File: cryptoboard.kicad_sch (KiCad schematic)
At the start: 12 parts, among them J1 USB_A, J2 BOOT, U1 STM32F103C8Tx, U2 LM317_SOT-223-3.3V

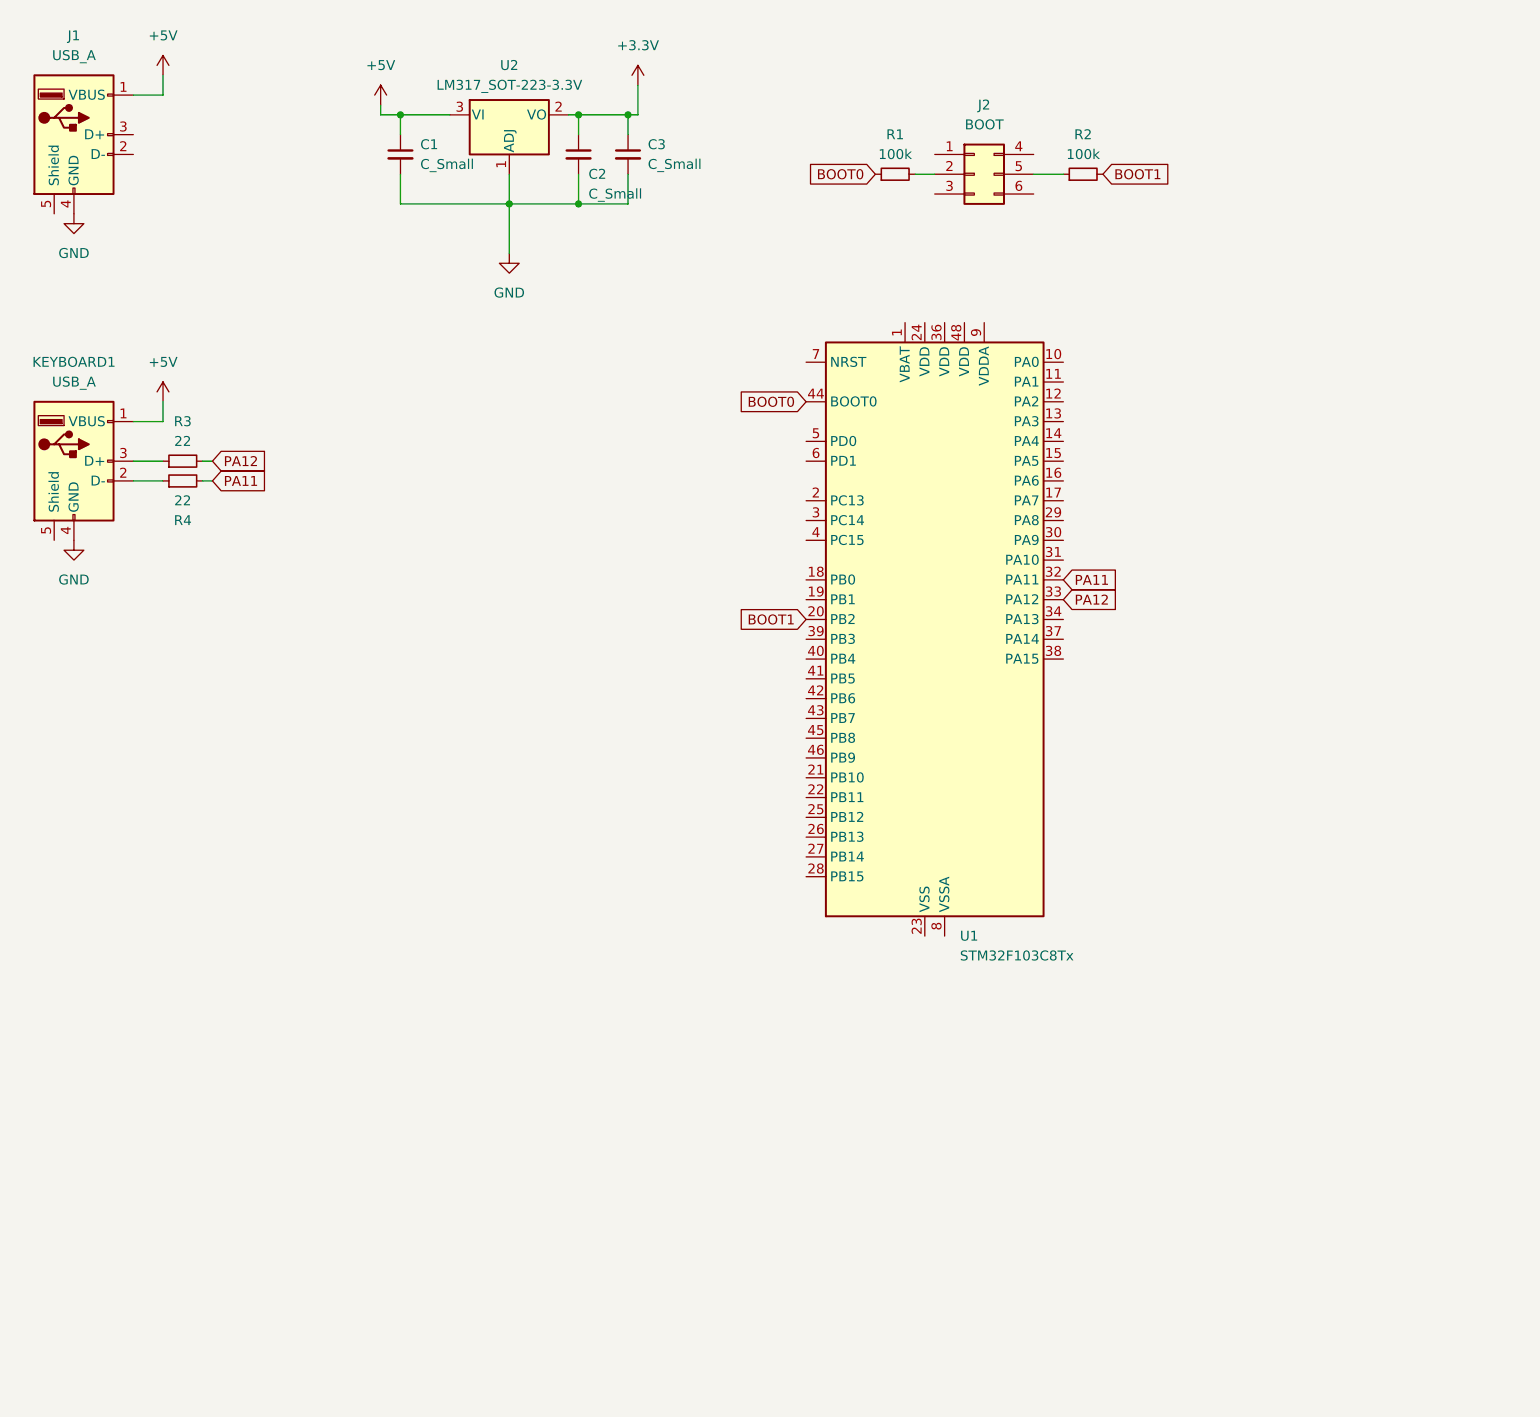
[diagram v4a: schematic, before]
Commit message: add stm32 capacitor
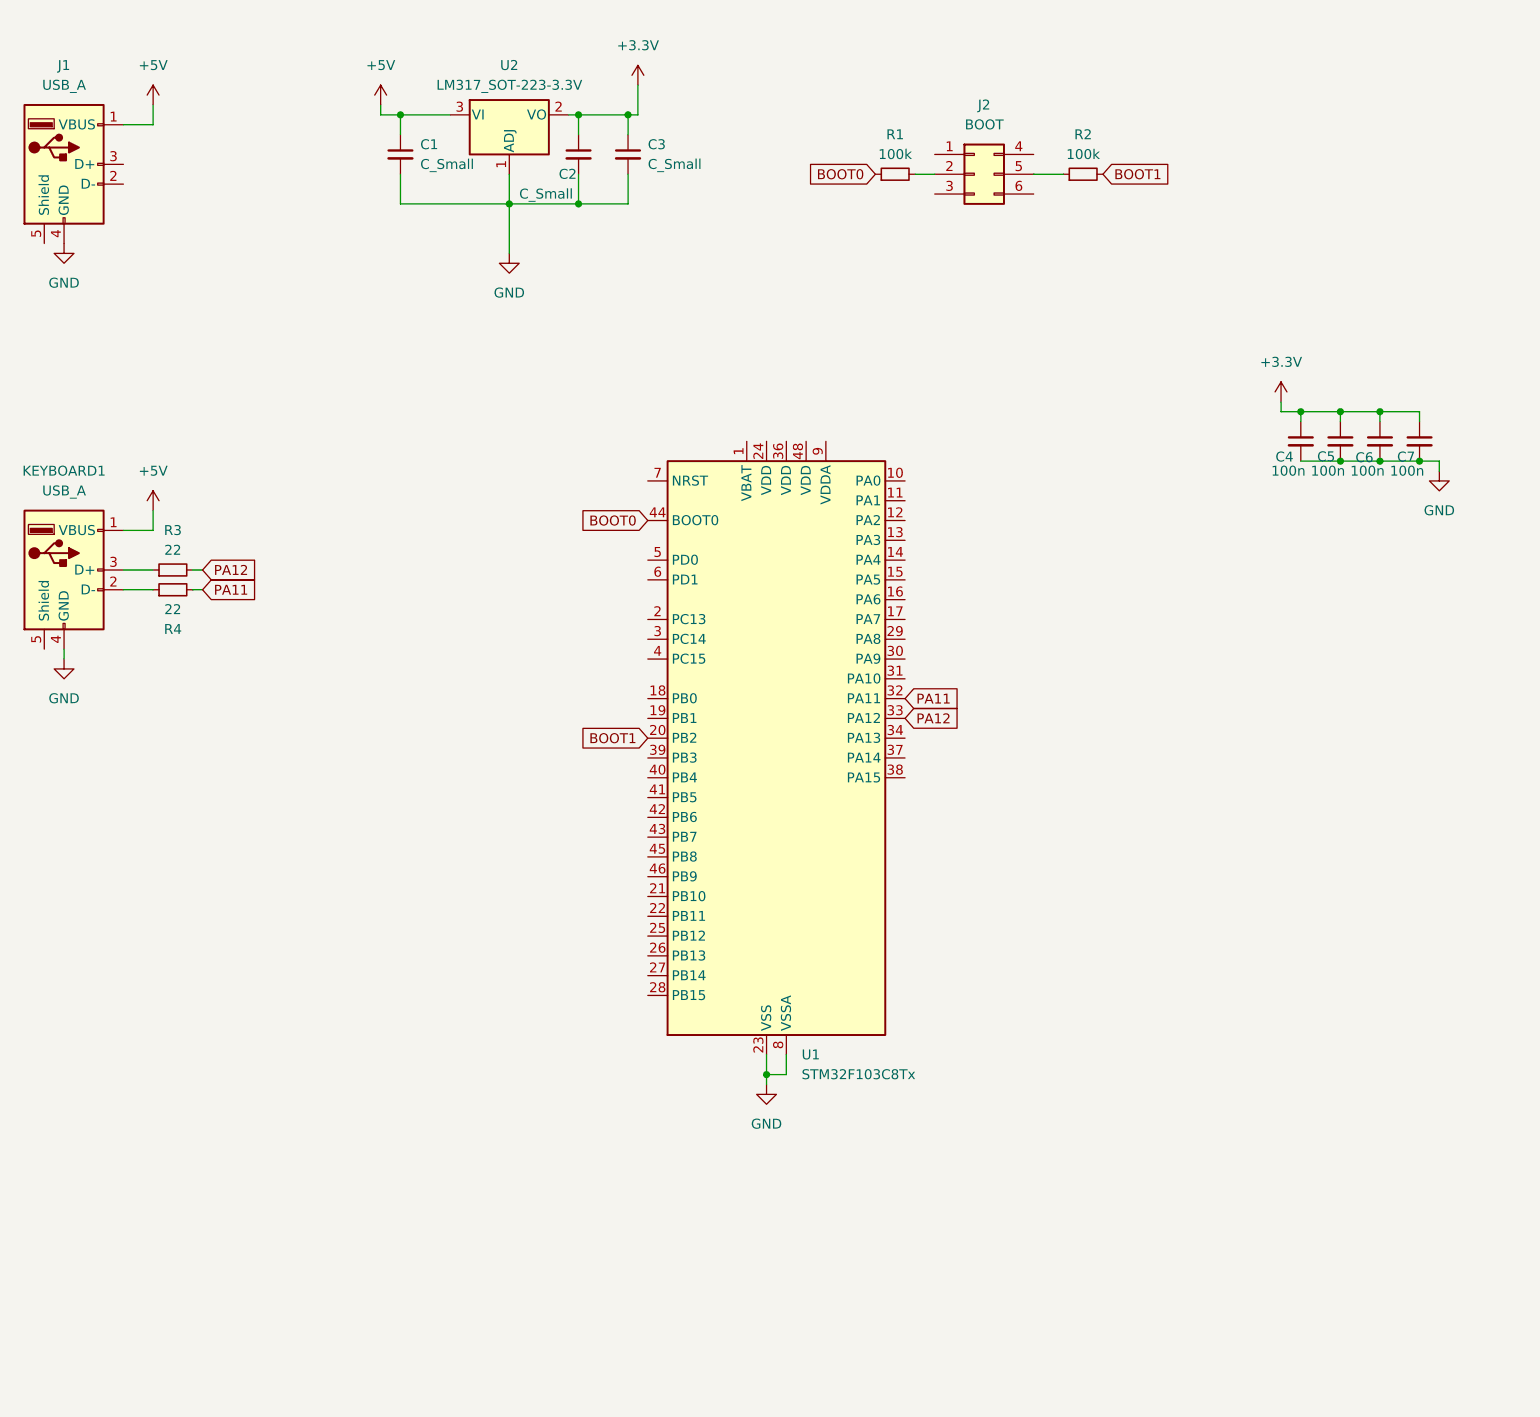
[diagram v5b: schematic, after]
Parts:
- added C4, C5, C6, C7: 100n, Capacitor_SMD:C_0603_1608Metric, symbol Device:C_Small
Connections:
- net +3.3V: now also C4.1, C5.1, C6.1, C7.1
- net GND: now also U1.23 (VSS), U1.35 (VSS), U1.47 (VSS), U1.8 (VSSA), C4.2, C5.2, C6.2, C7.2
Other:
- moved on the sheet: J1, KEYBOARD1, R3, R4, U1

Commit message: add swd
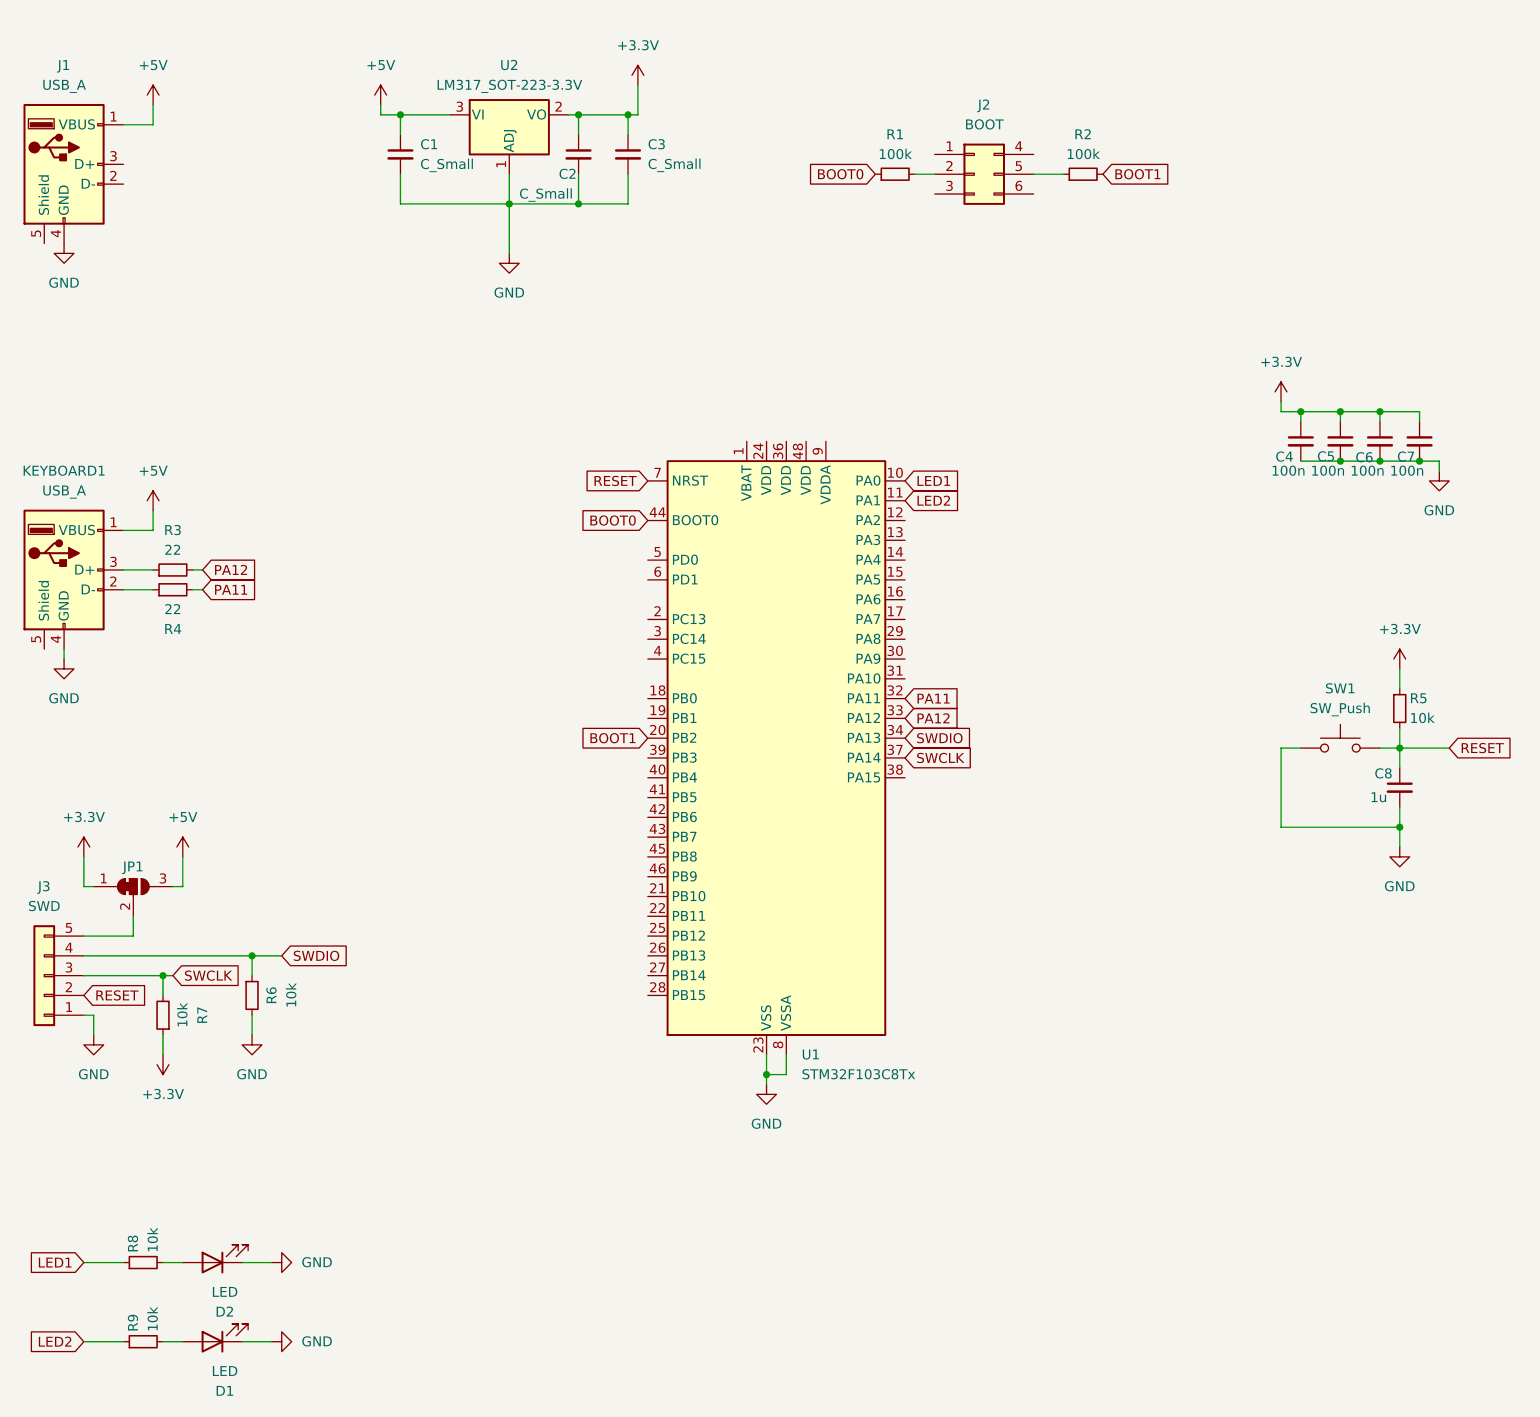
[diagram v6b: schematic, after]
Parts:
- added C8: 1u, Capacitor_SMD:C_0603_1608Metric, symbol Device:C_Small
- added D1, D2: LED, Diode_SMD:D_0603_1608Metric, symbol Device:LED
- added J3: SWD, Connector_PinHeader_2.54mm:PinHeader_1x05_P2.54mm_Vertical, symbol Connector_Generic:Conn_01x05
- added JP1: SolderJumper_3_Bridged12, Jumper:SolderJumper-3_P1.3mm_Bridged12_RoundedPad1.0x1.5mm, symbol Jumper:SolderJumper_3_Bridged12
- added R5, R6, R7, R8, R9: 10k, Resistor_SMD:R_0603_1608Metric, symbol Device:R_Small
- added SW1: SW_Push, Button_Switch_SMD:SW_SPST_CK_RS282G05A3, symbol Switch:SW_Push
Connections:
- net +3.3V: now also JP1.1 (A), R5.1, R7.1
- net +5V: now also JP1.3 (B)
- net GND: now also C8.2, D1.1 (K), D2.1 (K), J3.1 (Pin_1), R6.2, SW1.1
- net LED1: now reaches U1.10 (PA0)
- net LED1: now also R8.1
- net LED2: now reaches U1.11 (PA1)
- net LED2: now also R9.1
- net SWDIO: now reaches U1.34 (PA13)
- net SWDIO: now also J3.4 (Pin_4), R6.1
- net SWCLK: now reaches U1.37 (PA14)
- net SWCLK: now also J3.3 (Pin_3), R7.2
- net RESET: now reaches U1.7 (NRST)
- net RESET: now also C8.1, J3.2 (Pin_2), R5.2, SW1.2
- new net: D1.2 (A), R9.2
- new net: J3.5 (Pin_5), JP1.2 (C)
- new net: D2.2 (A), R8.2

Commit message: add vcc
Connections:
- net +3.3V: now also U1.1 (VBAT), U1.24 (VDD), U1.36 (VDD), U1.48 (VDD), U1.9 (VDDA)
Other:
- moved on the sheet: C4, C5, C6, C7, C8, R5, SW1, U1
